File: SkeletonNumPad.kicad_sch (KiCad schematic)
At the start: 68 parts, among them J1 USB_C_Receptacle_USB2.0, SW1 SW_PUSH, SW10 SW_PUSH, SW11 SW_PUSH, SW12 SW_PUSH, SW13 SW_PUSH, SW14 SW_PUSH, SW15 SW_PUSH, SW16 SW_PUSH, SW2 SW_PUSH, SW3 SW_PUSH, SW4 SW_PUSH, SW5 SW_PUSH, SW6 SW_PUSH, SW7 SW_PUSH, SW8 SW_PUSH, SW9 SW_PUSH, U1 ATmega32U4-M, Y1 Crystal_GND24

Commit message: Customize footprints
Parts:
- added D1: D_Small, Diode_SMD:D_SOD-123, symbol Device:D_Small
- added LED17: YS-SK6812MINI-E, keyboard:YS-SK6812MINI-E, symbol kbd:YS-SK6812MINI-E
- added SW1: SW_PUSH, Custom:MXOnly-1U-Hotswap, symbol kbd:SW_PUSH
- added U?: ATmega32U2-M, Package_DFN_QFN:QFN-32-1EP_5x5mm_P0.5mm_EP3.1x3.1mm, symbol MCU_Microchip_ATmega:ATmega32U2-M
- SW10: renamed from SW9; footprint MX_Only:MXOnly-1U-NoLED -> Custom:MXOnly-1U-Hotswap
- SW11: renamed from SW10; footprint MX_Only:MXOnly-1U-NoLED -> Custom:MXOnly-1U-Hotswap
- SW12: renamed from SW11; footprint MX_Only:MXOnly-1U-NoLED -> Custom:MXOnly-1U-Hotswap
- SW13: renamed from SW12; footprint MX_Only:MXOnly-1U-NoLED -> Custom:MXOnly-1U-Hotswap
- SW14: renamed from SW13; footprint MX_Only:MXOnly-1U-NoLED -> Custom:MXOnly-1U-Hotswap
- SW15: renamed from SW14; footprint MX_Only:MXOnly-2U-VerticalStabilizers-NoLED -> Custom:MXOnly-2U-Hotswap-VerticalStabilizers
- SW16: renamed from SW15; footprint MX_Only:MXOnly-2U-NoLED -> Custom:MXOnly-2U-Hotswap
- SW17: renamed from SW16; footprint MX_Only:MXOnly-1U-NoLED -> Custom:MXOnly-1U-Hotswap
- SW2: renamed from SW1; footprint MX_Only:MXOnly-1U-NoLED -> Custom:MXOnly-1U-Hotswap
- SW3: renamed from SW2; footprint MX_Only:MXOnly-1U-NoLED -> Custom:MXOnly-1U-Hotswap
- SW4: renamed from SW3; footprint MX_Only:MXOnly-1U-NoLED -> Custom:MXOnly-1U-Hotswap
- SW5: renamed from SW4; footprint MX_Only:MXOnly-1U-NoLED -> Custom:MXOnly-1U-Hotswap
- SW6: renamed from SW5; footprint MX_Only:MXOnly-1U-NoLED -> Custom:MXOnly-1U-Hotswap
- SW7: renamed from SW6; footprint MX_Only:MXOnly-1U-NoLED -> Custom:MXOnly-1U-Hotswap
- SW8: renamed from SW7; footprint MX_Only:MXOnly-2U-VerticalStabilizers-NoLED -> Custom:MXOnly-2U-Hotswap-VerticalStabilizers
- SW9: renamed from SW8; footprint MX_Only:MXOnly-1U-NoLED -> Custom:MXOnly-1U-Hotswap
- renumbered D9 to D10, D10 to D11, D11 to D12, D12 to D13, D13 to D14, D14 to D15, D15 to D16, D16 to D17, D1 to D2, D2 to D3, D3 to D4, D4 to D5, D5 to D6, D6 to D7, D7 to D8, D8 to D9, R2 to R1, R3 to R2, R4 to R3, R5 to R4, R6 to R5, R1 to R6
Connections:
- net +5V: now also LED17.1 (VDD)
- net GND: now also LED17.3 (VSS)
- net col0: now also SW1.1
- net row0: now also D1.1 (K)
- net at LED16.2 (DOUT): now also LED17.4 (DIN)
- new net: D1.2 (A), SW1.2
- new net: U?.3 (GND), U?.33 (GND)

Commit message: with WS2812B-2020
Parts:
- removed LED1, LED10, LED11, LED12, LED13, LED14, LED15, LED16, LED17, LED2, LED3, LED4, LED5, LED6, LED7, LED8, LED9: YS-SK6812MINI-E, keyboard:YS-SK6812MINI-E, symbol kbd:YS-SK6812MINI-E
- removed U?: ATmega32U2-M, Package_DFN_QFN:QFN-32-1EP_5x5mm_P0.5mm_EP3.1x3.1mm, symbol MCU_Microchip_ATmega:ATmega32U2-M
- added LED1, LED10, LED11, LED12, LED13, LED14, LED15, LED16, LED17, LED2, LED3, LED4, LED5, LED6, LED7, LED8, LED9: WS2812B, Custom:WS2812B-2020, symbol LED:WS2812B
- J1: footprint Connector_USB:USB_C_Receptacle_HRO_TYPE-C-31-M-12 -> Connector_USB:USB_C_Receptacle_Palconn_UTC16-G; LCSC C165948 -> C167321
- SW1, SW10, SW11, SW12, SW13, SW14, SW15, SW16, SW17, SW2, SW3, SW4, SW5, SW6, SW7, SW8, SW9: LCSC (none) -> C2803348
- U1: LCSC C45874 -> C112161
- U2: renamed from PRTR5V0U2X1; LCSC C12333 -> C2827688
- renumbered R5 to R4, R4 to R5, SW_RESET1 to SW_1
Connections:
- net +5V: now also LED1.1 (VDD), LED10.1 (VDD), LED11.1 (VDD), LED12.1 (VDD), LED13.1 (VDD), LED14.1 (VDD), LED15.1 (VDD), LED16.1 (VDD), LED17.1 (VDD), LED2.1 (VDD), LED3.1 (VDD), LED4.1 (VDD), LED5.1 (VDD), LED6.1 (VDD), LED7.1 (VDD), LED8.1 (VDD), LED9.1 (VDD)
- net GND: now also LED1.3 (VSS), LED10.3 (VSS), LED11.3 (VSS), LED12.3 (VSS), LED13.3 (VSS), LED14.3 (VSS), LED15.3 (VSS), LED16.3 (VSS), LED17.3 (VSS), LED2.3 (VSS), LED3.3 (VSS), LED4.3 (VSS), LED5.3 (VSS), LED6.3 (VSS), LED7.3 (VSS), LED8.3 (VSS), LED9.3 (VSS)
- net col0: now also U1.26 (PD6); no longer U1.40 (PF1)
- net col1: now also U1.27 (PD7); no longer U1.22 (PD5)
- net col2: now also U1.28 (PB4); no longer U1.21 (PD3)
- net col3: now also U1.29 (PB5); no longer U1.20 (PD2)
- net led: now also LED1.4 (DIN)
- net row0: now also U1.30 (PB6); no longer U1.26 (PD6)
- net row1: now also U1.31 (PC6); no longer U1.27 (PD7)
- net row2: now also U1.32 (PC7); no longer U1.28 (PB4)
- net row3: now also U1.36 (PF7); no longer U1.29 (PB5)
- net row4: now also U1.37 (PF6); no longer U1.30 (PB6)
- new net: LED13.2 (DOUT), LED14.4 (DIN)
- new net: LED12.2 (DOUT), LED13.4 (DIN)
- new net: LED6.2 (DOUT), LED7.4 (DIN)
- new net: LED5.2 (DOUT), LED6.4 (DIN)
- new net: LED1.2 (DOUT), LED2.4 (DIN)
- new net: LED11.2 (DOUT), LED12.4 (DIN)
- new net: LED10.2 (DOUT), LED11.4 (DIN)
- new net: LED7.2 (DOUT), LED8.4 (DIN)
- new net: LED15.2 (DOUT), LED16.4 (DIN)
- new net: LED14.2 (DOUT), LED15.4 (DIN)
- new net: LED16.2 (DOUT), LED17.4 (DIN)
- new net: LED10.4 (DIN), LED9.2 (DOUT)
- new net: LED8.2 (DOUT), LED9.4 (DIN)
- new net: LED4.2 (DOUT), LED5.4 (DIN)
- new net: LED3.2 (DOUT), LED4.4 (DIN)
- new net: LED2.2 (DOUT), LED3.4 (DIN)

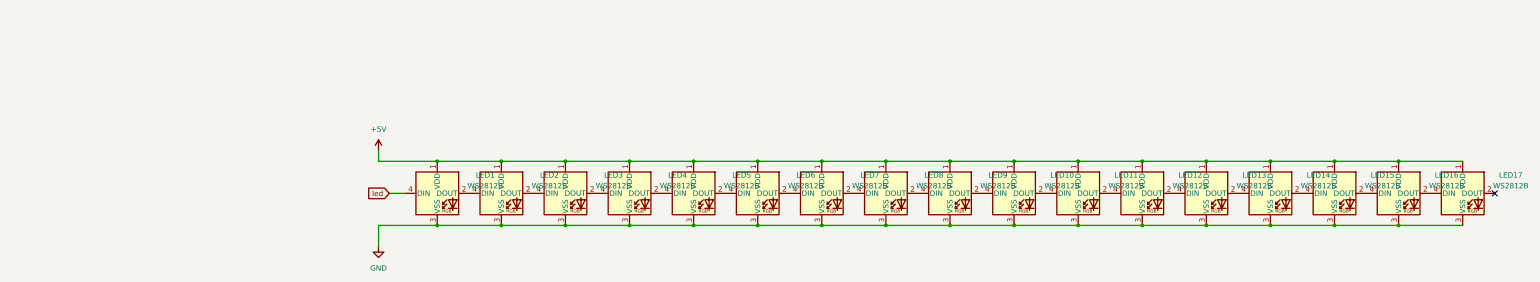
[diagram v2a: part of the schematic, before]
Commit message: with SK6812mini-e
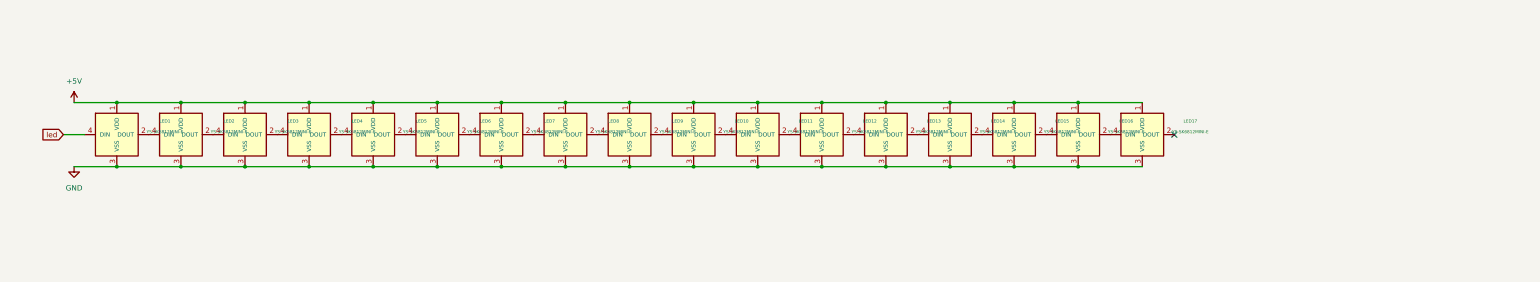
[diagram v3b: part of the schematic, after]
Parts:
- removed LED1, LED10, LED11, LED12, LED13, LED14, LED15, LED16, LED17, LED2, LED3, LED4, LED5, LED6, LED7, LED8, LED9: WS2812B, Custom:WS2812B-2020, symbol LED:WS2812B
- added LED1, LED10, LED11, LED12, LED13, LED14, LED15, LED16, LED17, LED2, LED3, LED4, LED5, LED6, LED7, LED8, LED9: YS-SK6812MINI-E, Custom:YS-SK6812MINI-E, symbol kbd:YS-SK6812MINI-E
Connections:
- net +5V: now also LED1.1 (VDD), LED10.1 (VDD), LED11.1 (VDD), LED12.1 (VDD), LED13.1 (VDD), LED14.1 (VDD), LED15.1 (VDD), LED16.1 (VDD), LED17.1 (VDD), LED2.1 (VDD), LED3.1 (VDD), LED4.1 (VDD), LED5.1 (VDD), LED6.1 (VDD), LED7.1 (VDD), LED8.1 (VDD), LED9.1 (VDD)
- net GND: now also LED1.3 (VSS), LED10.3 (VSS), LED11.3 (VSS), LED12.3 (VSS), LED13.3 (VSS), LED14.3 (VSS), LED15.3 (VSS), LED16.3 (VSS), LED17.3 (VSS), LED2.3 (VSS), LED3.3 (VSS), LED4.3 (VSS), LED5.3 (VSS), LED6.3 (VSS), LED7.3 (VSS), LED8.3 (VSS), LED9.3 (VSS)
- net led: now also LED1.4 (DIN)
- new net: LED3.2 (DOUT), LED4.4 (DIN)
- new net: LED2.2 (DOUT), LED3.4 (DIN)
- new net: LED6.2 (DOUT), LED7.4 (DIN)
- new net: LED5.2 (DOUT), LED6.4 (DIN)
- new net: LED1.2 (DOUT), LED2.4 (DIN)
- new net: LED16.2 (DOUT), LED17.4 (DIN)
- new net: LED15.2 (DOUT), LED16.4 (DIN)
- new net: LED10.4 (DIN), LED9.2 (DOUT)
- new net: LED8.2 (DOUT), LED9.4 (DIN)
- new net: LED14.2 (DOUT), LED15.4 (DIN)
- new net: LED13.2 (DOUT), LED14.4 (DIN)
- new net: LED12.2 (DOUT), LED13.4 (DIN)
- new net: LED11.2 (DOUT), LED12.4 (DIN)
- new net: LED7.2 (DOUT), LED8.4 (DIN)
- new net: LED4.2 (DOUT), LED5.4 (DIN)
- new net: LED10.2 (DOUT), LED11.4 (DIN)
